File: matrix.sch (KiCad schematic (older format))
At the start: 136 parts, among them K1 ESC, K10 SW_SPST, K11 SW_SPST, K12 SW_SPST, K13 SW_SPST, K14 SW_SPST, K15 SW_SPST, K16 SW_SPST, K17 SW_SPST, K18 SW_SPST, K19 SW_SPST, K2 SW_SPST, K20 SW_SPST, K21 SW_SPST, K22 SW_SPST, K23 SW_SPST, K24 SW_SPST, K25 SW_SPST, K26 SW_SPST, K27 SW_SPST, K28 SW_SPST, K29 SW_SPST, K3 SW_SPST, K30 SW_SPST, K31 SW_SPST, K32 SW_SPST, K33 SW_SPST, K34 SW_SPST, K35 SW_SPST, K36 SW_SPST, K37 SW_SPST, K38 SW_SPST, K39 SW_SPST, K4 SW_SPST, K40 SW_SPST, K41 SW_SPST, K42 SW_SPST, K43 SW_SPST, K44 SW_SPST, K45 SW_SPST, K46 SW_SPST, K47 SW_SPST, K48 SW_SPST, K49 SW_SPST, K5 SW_SPST, K50 SW_SPST, K51 SW_SPST, K52 SW_SPST, K53 SW_SPST, K54 SW_SPST, K55 SW_SPST, K56 SW_SPST, K57 SW_SPST, K58 SW_SPST, K59 SW_SPST, K6 SW_SPST, K60 SW_SPST, K61 SW_SPST, K62 SW_SPST, K63 SW_SPST, K64 SW_SPST, K65 SW_SPST, K66 SW_SPST, K67 SW_SPST, K68 SW_SPST, K7 SW_SPST, K8 SW_SPST, K9 SW_SPST

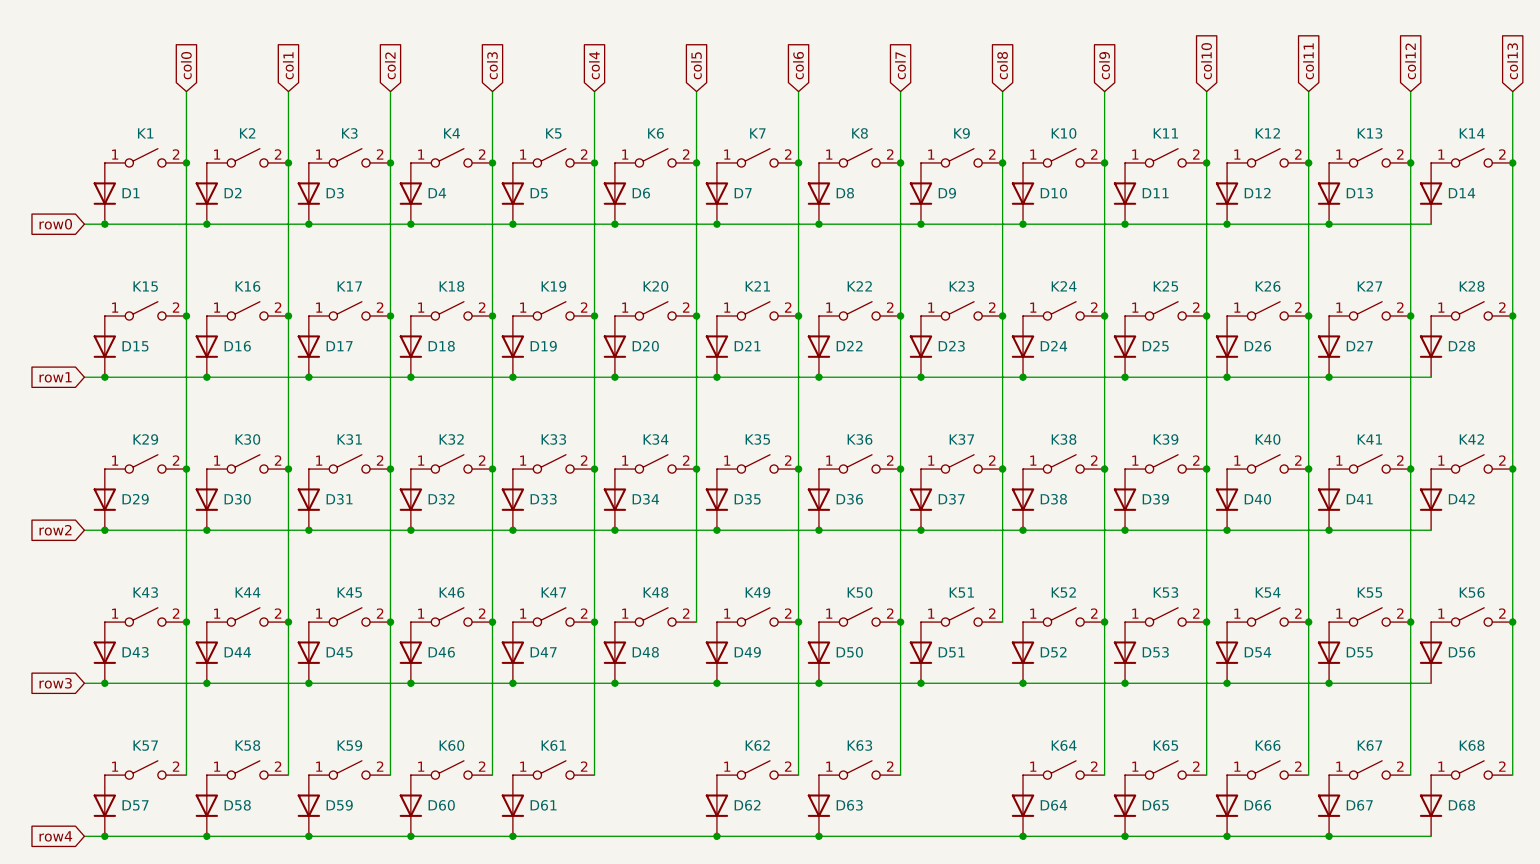
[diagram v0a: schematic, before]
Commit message: Tweak matrix back to 18 pins
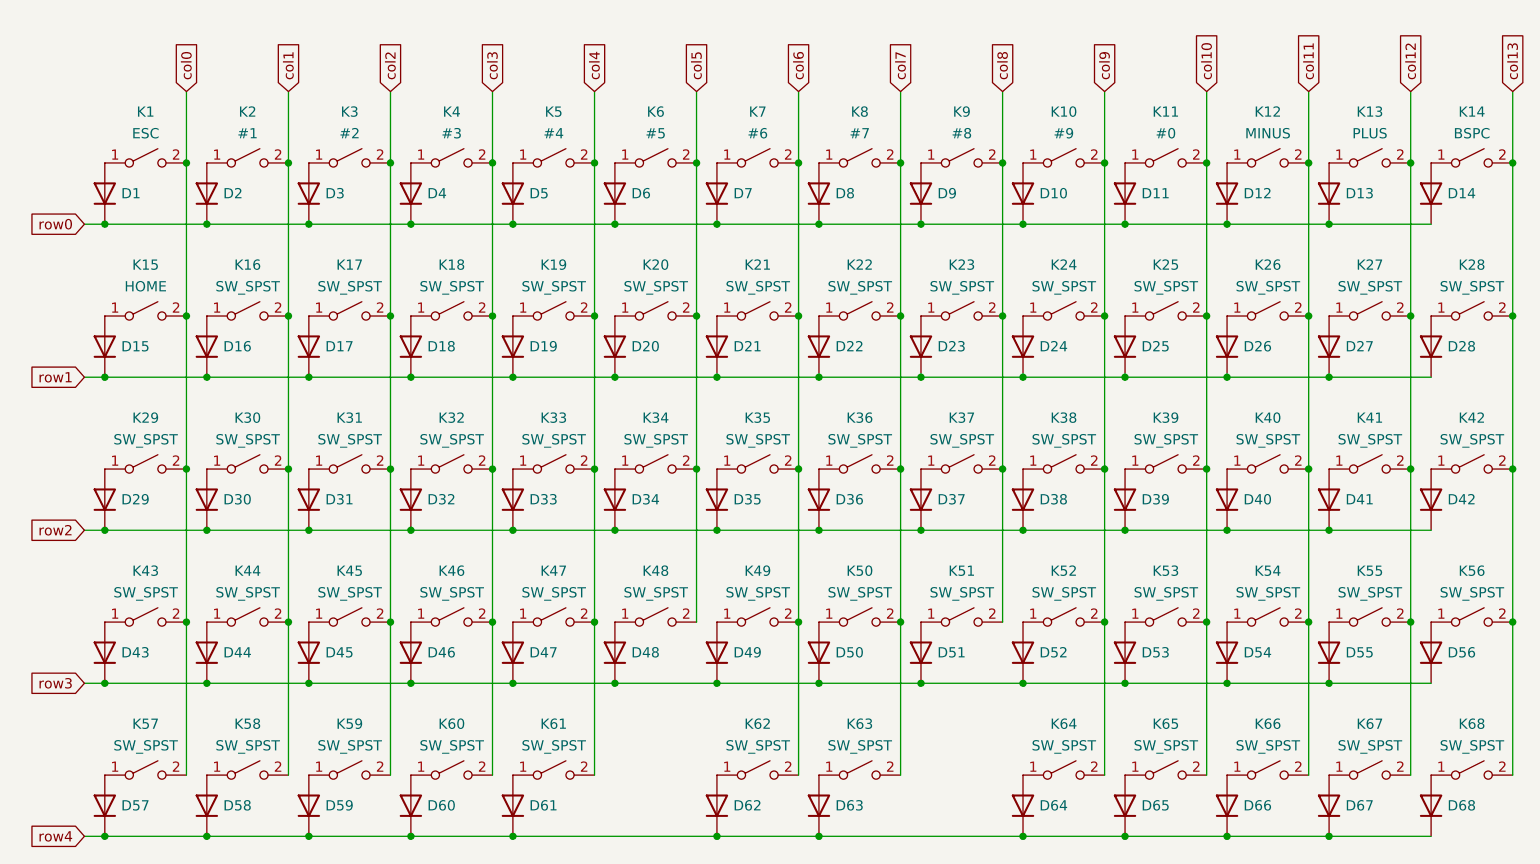
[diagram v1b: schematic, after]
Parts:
- K10: value SW_SPST -> #9
- K11: value SW_SPST -> #0
- K12: value SW_SPST -> MINUS
- K13: value SW_SPST -> PLUS
- K14: value SW_SPST -> BSPC
- K15: value SW_SPST -> HOME
- K2: value SW_SPST -> #1
- K3: value SW_SPST -> #2
- K4: value SW_SPST -> #3
- K5: value SW_SPST -> #4
- K6: value SW_SPST -> #5
- K7: value SW_SPST -> #6
- K8: value SW_SPST -> #7
- K9: value SW_SPST -> #8

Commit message: Labeled all keys
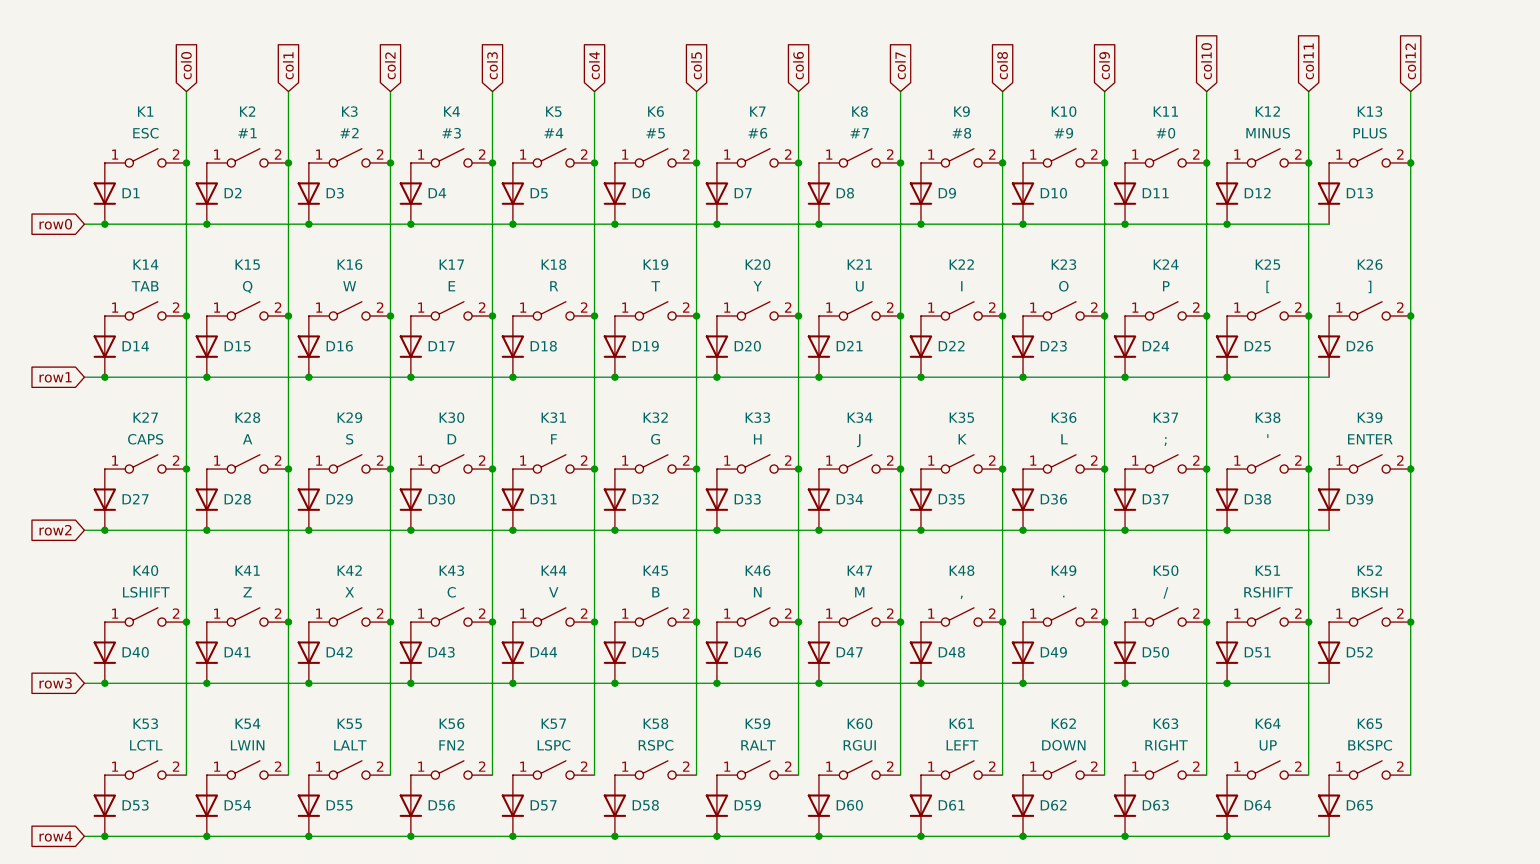
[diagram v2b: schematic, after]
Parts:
- removed D14, D28, D42, D56, D68: D, symbol Device:D
- removed K14: BSPC, symbol Switch:SW_SPST
- removed K28, K42, K56, K68: SW_SPST, symbol Switch:SW_SPST
- added D58, D61: D, symbol Device:D
- added K58: RSPC, symbol Switch:SW_SPST
- added K61: LEFT, symbol Switch:SW_SPST
- K14: renamed from K15; value HOME -> TAB
- K15: renamed from K16; value SW_SPST -> Q
- K16: renamed from K17; value SW_SPST -> W
- K17: renamed from K18; value SW_SPST -> E
- K18: renamed from K19; value SW_SPST -> R
- K19: renamed from K20; value SW_SPST -> T
- K20: renamed from K21; value SW_SPST -> Y
- K21: renamed from K22; value SW_SPST -> U
- K22: renamed from K23; value SW_SPST -> I
- K23: renamed from K24; value SW_SPST -> O
- K24: renamed from K25; value SW_SPST -> P
- K25: renamed from K26; value SW_SPST -> [
- K26: renamed from K27; value SW_SPST -> ]
- K27: renamed from K29; value SW_SPST -> CAPS
- K28: renamed from K30; value SW_SPST -> A
- K29: renamed from K31; value SW_SPST -> S
- K30: renamed from K32; value SW_SPST -> D
- K31: renamed from K33; value SW_SPST -> F
- K32: renamed from K34; value SW_SPST -> G
- K33: renamed from K35; value SW_SPST -> H
- K34: renamed from K36; value SW_SPST -> J
- K35: renamed from K37; value SW_SPST -> K
- K36: renamed from K38; value SW_SPST -> L
- K37: renamed from K39; value SW_SPST -> ;
- K38: renamed from K40; value SW_SPST -> '
- K39: renamed from K41; value SW_SPST -> ENTER
- K40: renamed from K43; value SW_SPST -> LSHIFT
- K41: renamed from K44; value SW_SPST -> Z
- K42: renamed from K45; value SW_SPST -> X
- K43: renamed from K46; value SW_SPST -> C
- K44: renamed from K47; value SW_SPST -> V
- K45: renamed from K48; value SW_SPST -> B
- K46: renamed from K49; value SW_SPST -> N
- K47: renamed from K50; value SW_SPST -> M
- K48: renamed from K51; value SW_SPST -> ,
- K49: renamed from K52; value SW_SPST -> .
- K50: renamed from K53; value SW_SPST -> /
- K51: renamed from K54; value SW_SPST -> RSHIFT
- K52: renamed from K55; value SW_SPST -> BKSH
- K53: renamed from K57; value SW_SPST -> LCTL
- K54: renamed from K58; value SW_SPST -> LWIN
- K55: renamed from K59; value SW_SPST -> LALT
- K56: renamed from K60; value SW_SPST -> FN2
- K57: renamed from K61; value SW_SPST -> LSPC
- K59: renamed from K62; value SW_SPST -> RALT
- K60: renamed from K63; value SW_SPST -> RGUI
- K62: renamed from K64; value SW_SPST -> DOWN
- K63: renamed from K65; value SW_SPST -> RIGHT
- K64: renamed from K66; value SW_SPST -> UP
- K65: renamed from K67; value SW_SPST -> BKSPC
- renumbered D15 to D14, D16 to D15, D17 to D16, D18 to D17, D19 to D18, D20 to D19, D21 to D20, D22 to D21, D23 to D22, D24 to D23, D25 to D24, D26 to D25, D27 to D26, D29 to D27, D30 to D28, D31 to D29, D32 to D30, D33 to D31, D34 to D32, D35 to D33, D36 to D34, D37 to D35, D38 to D36, D39 to D37, D40 to D38, D41 to D39, D43 to D40, D44 to D41, D45 to D42, D46 to D43, D47 to D44, D48 to D45, D49 to D46, D50 to D47, D51 to D48, D52 to D49, D53 to D50, D54 to D51, D55 to D52, D57 to D53, D58 to D54, D59 to D55, D60 to D56, D61 to D57, D62 to D59, D63 to D60, D64 to D62, D65 to D63, D66 to D64, D67 to D65
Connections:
- net col5: now also K58.2 (B)
- net col8: now also K61.2 (B)
- net row4: now also D58.1 (K), D61.1 (K)
- new net: D61.2 (A), K61.1 (A)
- new net: D58.2 (A), K58.1 (A)

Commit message: Arranged a large amount of switches
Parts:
- D1, D10, D11, D12, D13, D14, D15, D16, D17, D18, D19, D2, D20, D21, D22, D23, D24, D25, D26, D27, D28, D29, D3, D30, D31, D32, D33, D34, D35, D36, D37, D38, D39, D4, D40, D41, D42, D43, D44, D45, D46, D47, D48, D49, D5, D50, D51, D52, D53, D54, D55, D56, D57, D58, D59, D6, D60, D61, D62, D63, D64, D65, D7, D8, D9: footprint (none) -> Diode_THT:D_DO-34_SOD68_P10.16mm_Horizontal
- K1, K10, K11, K12, K13, K14, K15, K16, K17, K18, K19, K2, K20, K21, K22, K23, K24, K25, K26, K27, K28, K29, K3, K30, K31, K32, K33, K34, K35, K36, K37, K38, K4, K41, K42, K43, K44, K45, K46, K47, K48, K49, K5, K50, K51, K52, K53, K54, K55, K56, K59, K6, K60, K61, K62, K63, K64, K7, K8, K9: footprint (none) -> Keebio-Parts:MX-Alps-Choc-1U-NoLED
- K39, K40, K57, K58, K65: footprint (none) -> Keebio-Parts:MX-Alps-Choc-2U

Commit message: Wip: row stagger is wrong!
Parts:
- K40: footprint Keebio-Parts:MX-Alps-Choc-2U -> xeal_components:MX-Alps-Choc-2U-pin-flip
- K61, K62, K63: footprint Keebio-Parts:MX-Alps-Choc-1U-NoLED -> xeal_components:MX-Alps-Choc-1U-NoLED-PinSwap
- K65: footprint Keebio-Parts:MX-Alps-Choc-2U -> xeal_components:MX-Alps-Choc-2U-no-led
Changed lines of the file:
@@
 F 0 "K40" H 2050 4400 50  0000 C CNN
 F 1 "LSHIFT" H 2050 4294 50  0000 C CNN
-F 2 "Keebio-Parts:MX-Alps-Choc-2U" H 2050 4150 50  0001 C CNN
+F 2 "xeal_components:MX-Alps-Choc-2U-pin-flip" H 2050 4150 50  0001 C CNN
 F 3 "~" H 2050 4150 50  0001 C CNN
 	1    2050 4150
@@
 F 0 "K62" H 6550 5150 50  0000 C CNN
 F 1 "DOWN" H 6550 5044 50  0000 C CNN
-F 2 "Keebio-Parts:MX-Alps-Choc-1U-NoLED" H 6550 4900 50  0001 C CNN
+F 2 "xeal_components:MX-Alps-Choc-1U-NoLED-PinSwap" H 6550 4900 50  0001 C CNN
 F 3 "~" H 6550 4900 50  0001 C CNN
 	1    6550 4900
@@
 F 0 "K63" H 7050 5150 50  0000 C CNN
 F 1 "RIGHT" H 7050 5044 50  0000 C CNN
-F 2 "Keebio-Parts:MX-Alps-Choc-1U-NoLED" H 7050 4900 50  0001 C CNN
+F 2 "xeal_components:MX-Alps-Choc-1U-NoLED-PinSwap" H 7050 4900 50  0001 C CNN
 F 3 "~" H 7050 4900 50  0001 C CNN
 	1    7050 4900
@@
 F 0 "K65" H 8050 5150 50  0000 C CNN
 F 1 "BKSPC" H 8050 5044 50  0000 C CNN
-F 2 "Keebio-Parts:MX-Alps-Choc-2U" H 8050 4900 50  0001 C CNN
+F 2 "xeal_components:MX-Alps-Choc-2U-no-led" H 8050 4900 50  0001 C CNN
 F 3 "~" H 8050 4900 50  0001 C CNN
 	1    8050 4900
@@
 F 0 "K61" H 6050 5150 50  0000 C CNN
 F 1 "LEFT" H 6050 5044 50  0000 C CNN
-F 2 "Keebio-Parts:MX-Alps-Choc-1U-NoLED" H 6050 4900 50  0001 C CNN
+F 2 "xeal_components:MX-Alps-Choc-1U-NoLED-PinSwap" H 6050 4900 50  0001 C CNN
 F 3 "~" H 6050 4900 50  0001 C CNN
 	1    6050 4900

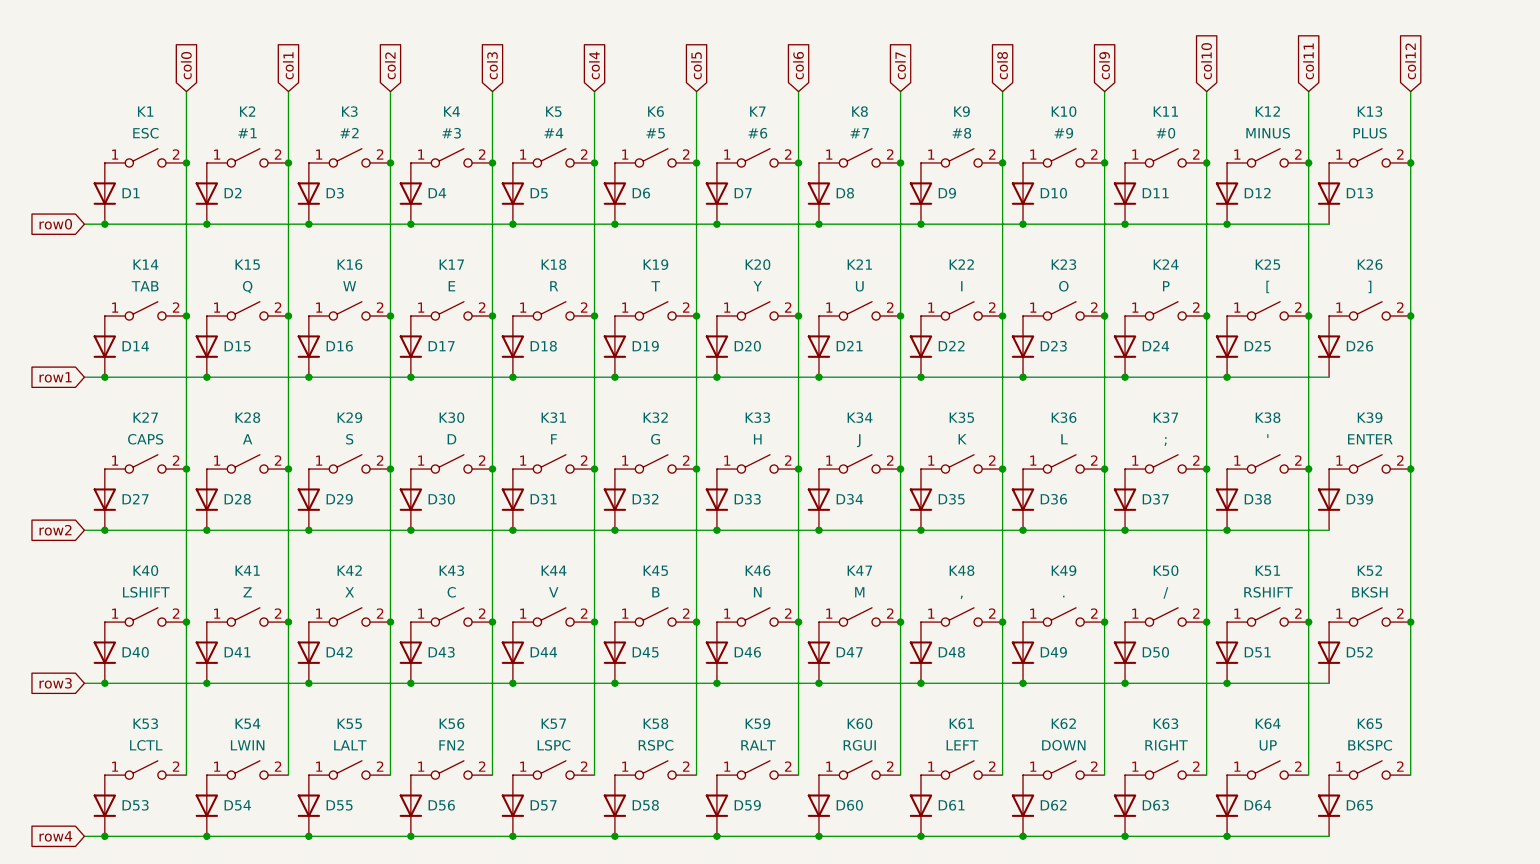
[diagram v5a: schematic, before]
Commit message: Fixed annotations, Only missing battery dip switch
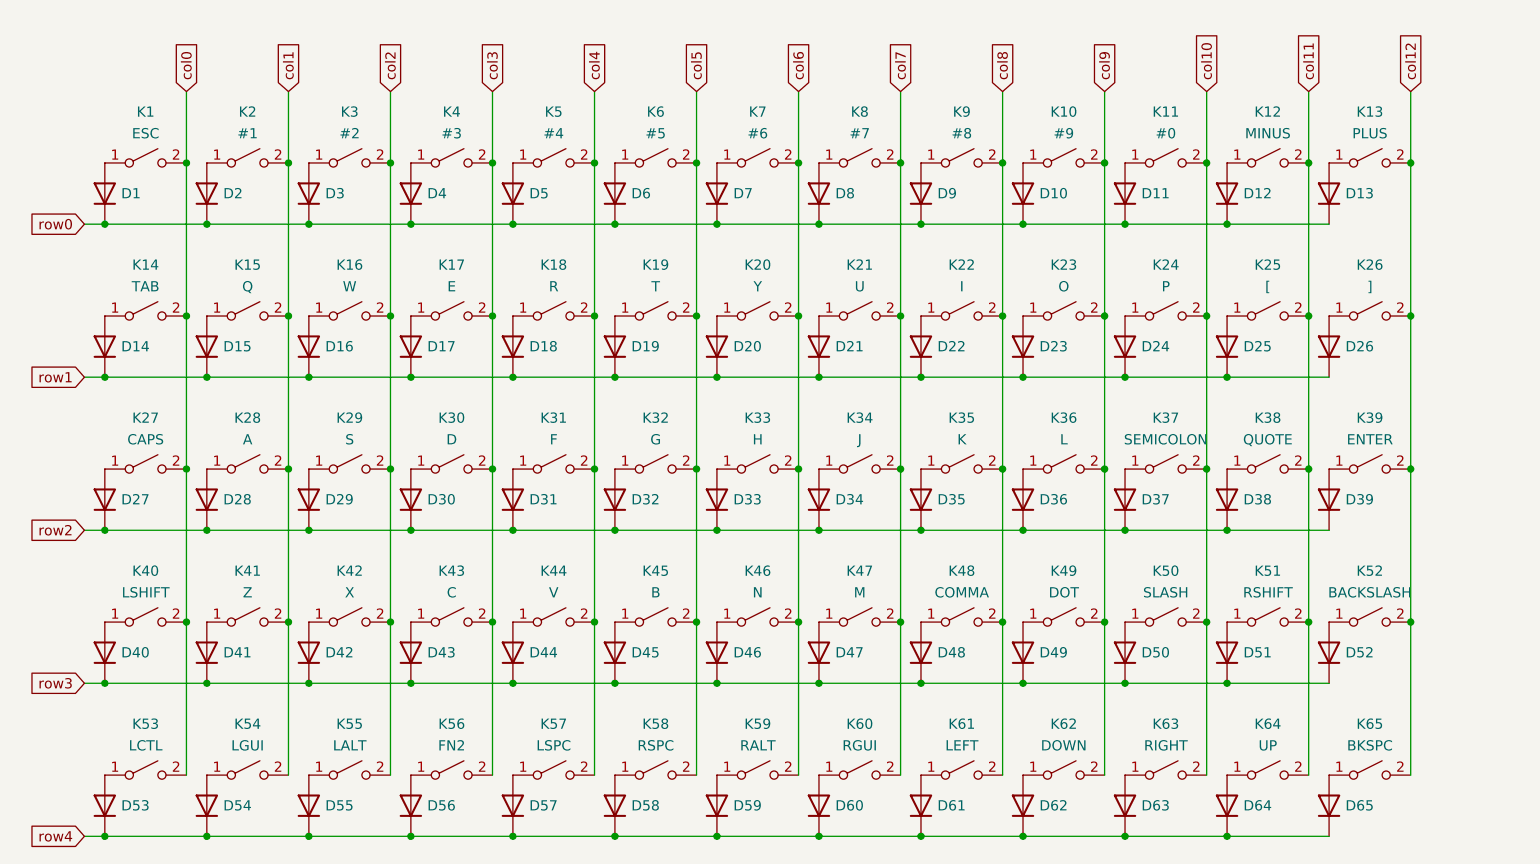
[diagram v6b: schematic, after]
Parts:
- D1, D10, D11, D12, D13, D14, D15, D16, D17, D18, D19, D2, D20, D21, D22, D23, D24, D25, D26, D27, D28, D29, D3, D30, D31, D32, D33, D34, D35, D36, D37, D38, D39, D4, D40, D41, D42, D43, D44, D45, D46, D47, D48, D49, D5, D50, D51, D52, D53, D54, D55, D56, D57, D58, D59, D6, D60, D61, D62, D63, D64, D65, D7, D8, D9: footprint Diode_THT:D_DO-34_SOD68_P10.16mm_Horizontal -> xeal_components:D_DO-34_SOD68_P10.16mm_Horizontal_NoK
- K1, K10, K11, K12, K13, K14, K15, K16, K17, K18, K19, K2, K20, K21, K22, K23, K24, K25, K26, K27, K28, K29, K3, K30, K31, K32, K33, K34, K35, K36, K4, K41, K42, K43, K44, K45, K46, K47, K5, K51, K53, K55, K56, K59, K6, K60, K64, K7, K8, K9: footprint Keebio-Parts:MX-Alps-Choc-1U-NoLED -> xeal_components:MX-Choc-1U
- K37: value ; -> SEMICOLON; footprint Keebio-Parts:MX-Alps-Choc-1U-NoLED -> xeal_components:MX-Choc-1U
- K38: value ' -> QUOTE; footprint Keebio-Parts:MX-Alps-Choc-1U-NoLED -> xeal_components:MX-Choc-1U
- K39, K57, K58: footprint Keebio-Parts:MX-Alps-Choc-2U -> xeal_components:MX-Alps-Choc-2U-no-led
- K48: value , -> COMMA; footprint Keebio-Parts:MX-Alps-Choc-1U-NoLED -> xeal_components:MX-Choc-1U
- K49: value . -> DOT; footprint Keebio-Parts:MX-Alps-Choc-1U-NoLED -> xeal_components:MX-Choc-1U
- K50: value / -> SLASH; footprint Keebio-Parts:MX-Alps-Choc-1U-NoLED -> xeal_components:MX-Choc-1U
- K52: value BKSH -> BACKSLASH; footprint Keebio-Parts:MX-Alps-Choc-1U-NoLED -> xeal_components:MX-Choc-1U
- K54: value LWIN -> LGUI; footprint Keebio-Parts:MX-Alps-Choc-1U-NoLED -> xeal_components:MX-Choc-1U
- K61, K62, K63: footprint xeal_components:MX-Alps-Choc-1U-NoLED-PinSwap -> xeal_components:MX-Choc-1U-pin-flip
